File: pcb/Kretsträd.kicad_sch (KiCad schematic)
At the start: 56 parts, among them J1 Conn_01x02_Female, J2 Conn_01x02_Female, SW1 SW_PUSH, SW10 SW_PUSH, SW11 SW_PUSH, SW12 SW_PUSH, SW13 SW_PUSH, SW14 SW_PUSH, SW15 SW_PUSH, SW16 SW_PUSH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

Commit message: Traces completely re-routed.
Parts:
- removed Bat+_1, BatGND_1: MountingHole_Pad, kbd:1pin_conn, symbol Mechanical:MountingHole_Pad
- added J3: Conn_01x02_Female, Connector_Molex:Molex_PicoBlade_53047-0210_1x02_P1.25mm_Vertical, symbol Connector:Conn_01x02_Female
- added TH5: HOLE, MountingHole:MountingHole_3.2mm_M3, symbol SofleKeyboard-rescue:HOLE-Lily58-cache-Lily58_Pro-rescue
- D1, D10, D11, D12, D13, D14, D15, D16, D17, D2, D3, D4, D5, D6, D7, D8, D9: footprint jw_custom:Diode_SOD123_through_hole -> jw_custom_footprint:D_SOD123_THT
- J1: renamed from J2; footprint jw_custom_footprint:MOLEX_1x02_1.25mm_51146 -> Connector_Molex:Molex_Panelmate_53780-0270_1x02-1MP_P1.25mm_Horizontal
- J2: renamed from J1; footprint jw_custom_footprint:MOLEX_1x02_1.25mm_51146 -> Connector_Molex:Molex_Panelmate_53780-0270_1x02-1MP_P1.25mm_Horizontal
- JP2, JP3: value Hole_2 -> Hole_1
- JP4, JP5: value Hole_1 -> Hole_2
- SW_POWER_1, SW_POWER_2: footprint jw_custom_footprint:SPDT_C128955 -> Button_Switch_SMD:SW_SPDT_PCM12
- renumbered Hole_2 to Hole_1, Hole_1 to Hole_2
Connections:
- net Hole_1: now reaches Hole_1.1, JP2.1, JP3.1
- net Hole_1: now also J3.1 (Pin_1)
- net Hole_2: now reaches Hole_2.1, JP4.1, JP5.1
- net Hole_2: now also J3.2 (Pin_2)
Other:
- moved on the sheet: Hole_1, Hole_2, J2

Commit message: Tones of changes.
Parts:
- added JP1: to_RAW, Jumper:SolderJumper-2_P1.3mm_Open_RoundedPad1.0x1.5mm, symbol Device:Jumper_NO_Small
- D1, D10, D11, D12, D13, D14, D15, D16, D17, D2, D3, D4, D5, D6, D7, D8, D9: footprint jw_custom_footprint:D_SOD123_THT -> jw_custom_footprint:Diode_SOD123_THT_2
- JP2: renamed from JP1; footprint Jumper:SolderJumper-2_P1.3mm_Open_TrianglePad1.0x1.5mm -> Jumper:SolderJumper-2_P1.3mm_Open_RoundedPad1.0x1.5mm
- JP3: renamed from JP5; value Hole_2 -> Hole_1; footprint Jumper:SolderJumper-2_P1.3mm_Open_TrianglePad1.0x1.5mm -> Jumper:SolderJumper-2_P1.3mm_Open_RoundedPad1.0x1.5mm
- JP4: renamed from JP2; footprint Jumper:SolderJumper-2_P1.3mm_Open_TrianglePad1.0x1.5mm -> Jumper:SolderJumper-2_P1.3mm_Open_RoundedPad1.0x1.5mm
- JP5: renamed from JP4; footprint Jumper:SolderJumper-2_P1.3mm_Open_TrianglePad1.0x1.5mm -> Jumper:SolderJumper-2_P1.3mm_Open_RoundedPad1.0x1.5mm
- JP6: renamed from JP3; value Hole_1 -> Hole_2; footprint Jumper:SolderJumper-2_P1.3mm_Open_TrianglePad1.0x1.5mm -> Jumper:SolderJumper-2_P1.3mm_Open_RoundedPad1.0x1.5mm
- renumbered SW_POWER_1 to PWR_SW_1, SW_POWER_2 to PWR_SW_2
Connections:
- net Hole_1: now also JP3.1; no longer JP6.1
- net Hole_2: now also JP6.1; no longer JP3.1
- net RAW: now also JP1.2
- net at JP2.1, JP4.2, JP5.2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: now also JP1.1
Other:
- moved on the sheet: BT1, BT2, Hole_1, Hole_2, J1, J2, J3, JP2, JP3, JP4, JP5, JP6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

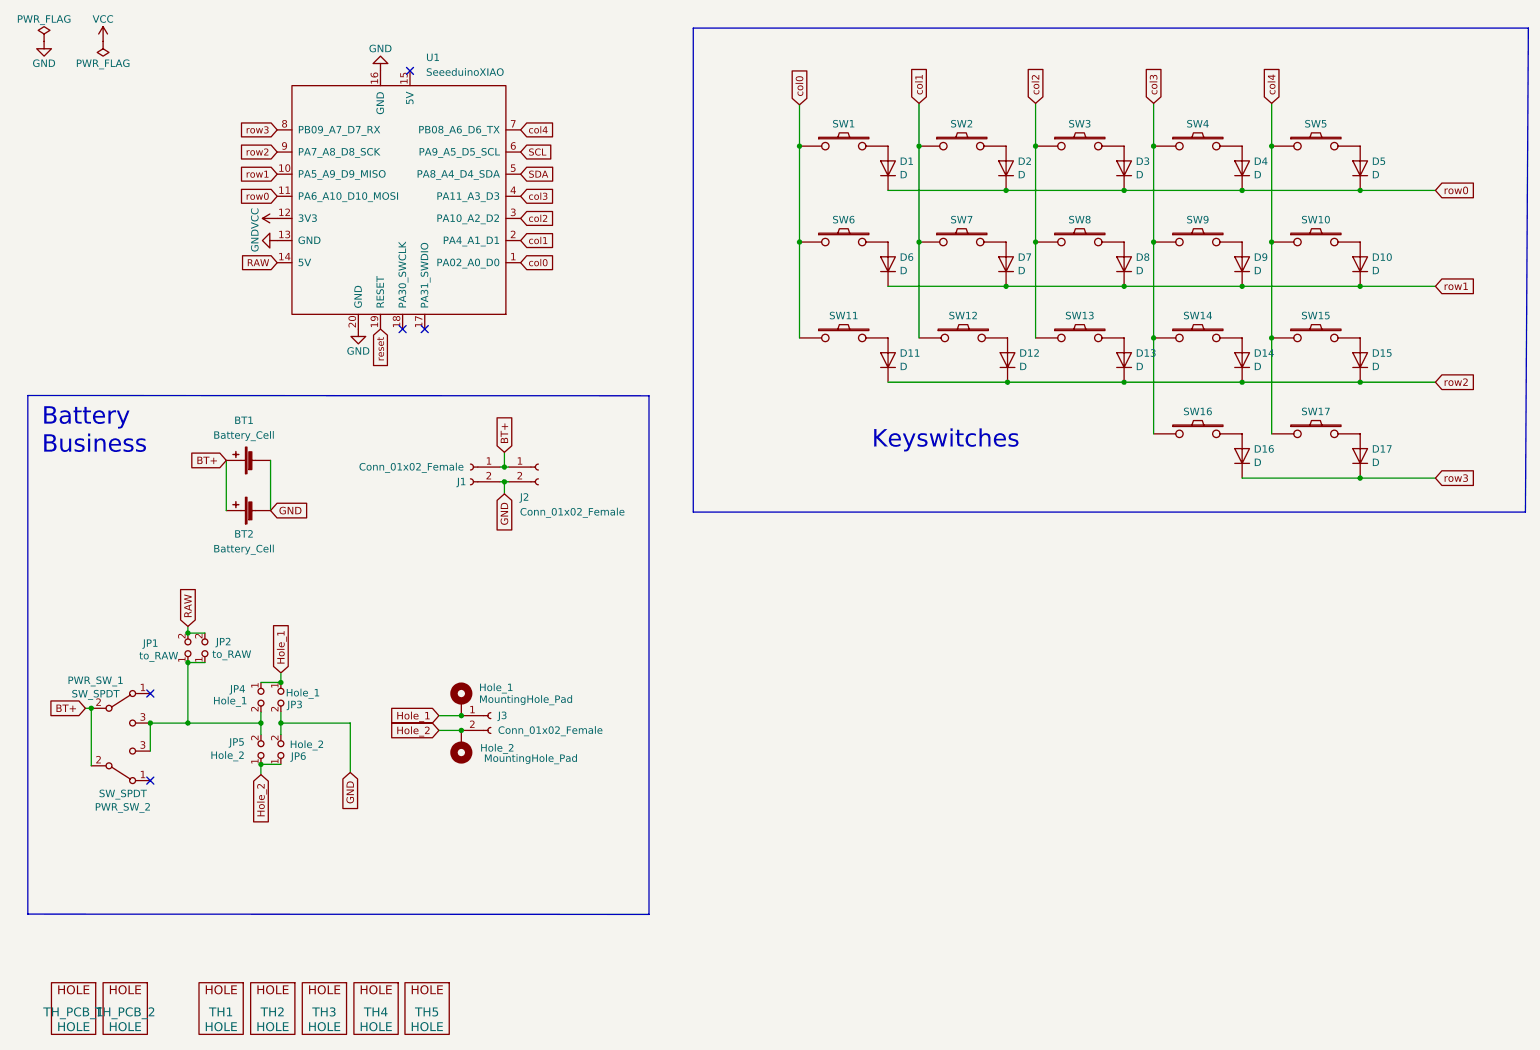
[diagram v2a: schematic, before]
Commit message: 1. Corrected all vias' size. 2. Minor change to circuit tree logo and text. 3. Other changes for aesthetics reasons.
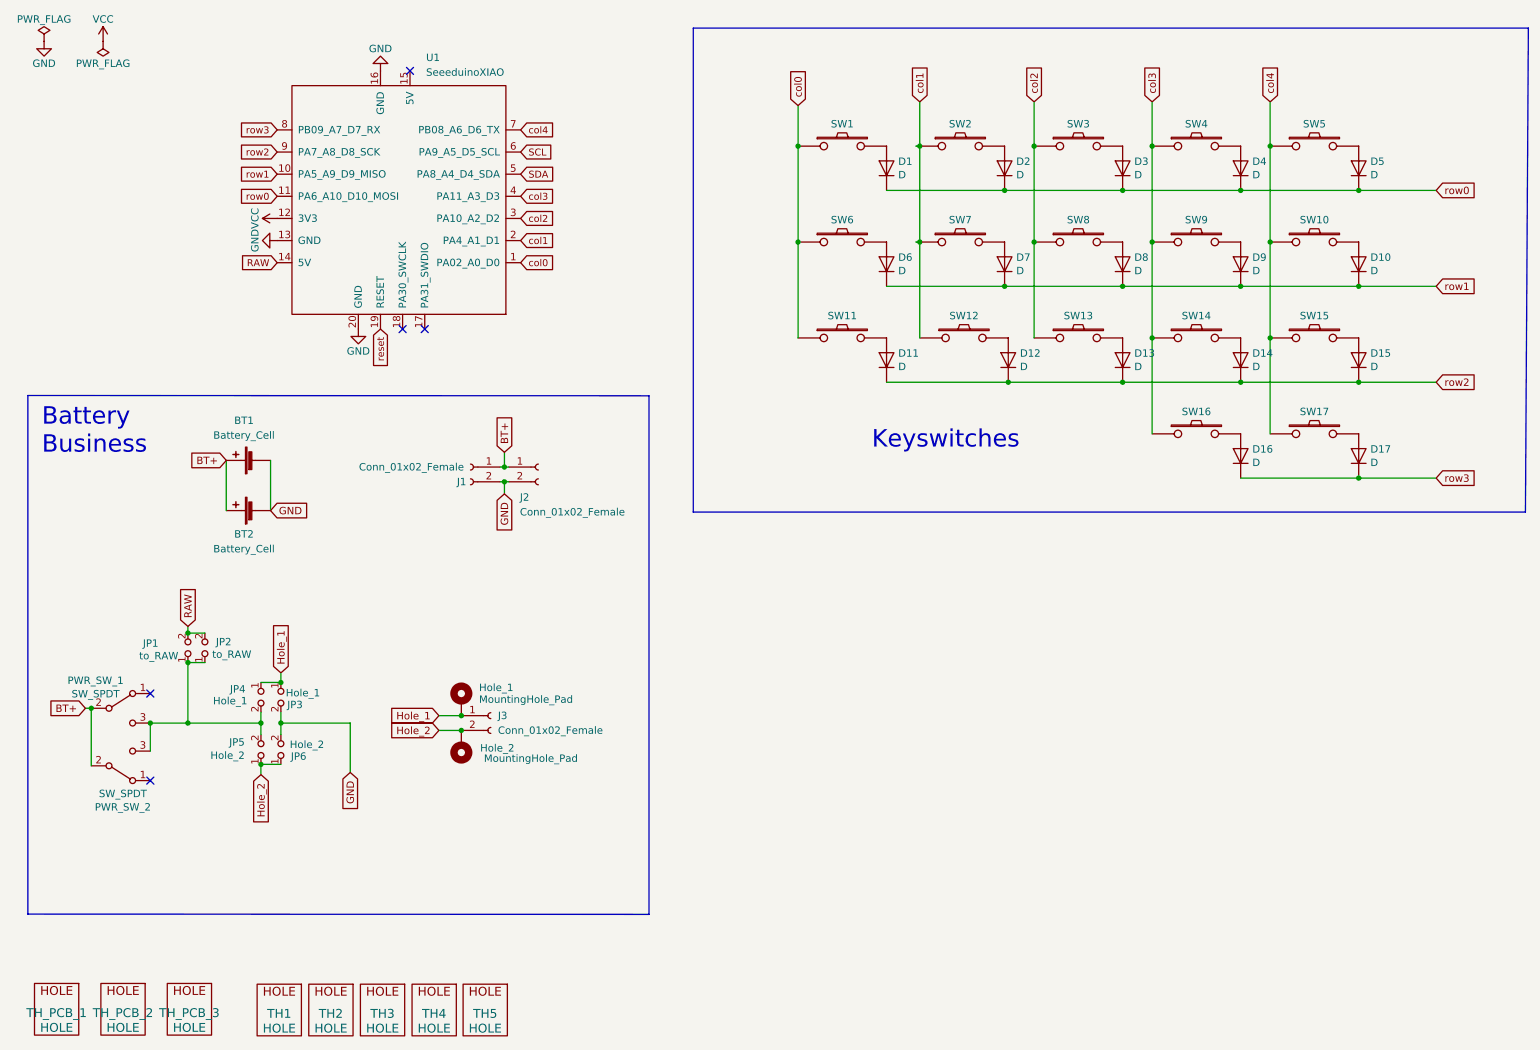
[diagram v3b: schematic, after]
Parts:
- added TH_PCB_3: HOLE, MountingHole:MountingHole_2.2mm_M2_Pad, symbol SofleKeyboard-rescue:HOLE-Lily58-cache-Lily58_Pro-rescue
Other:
- moved on the sheet: TH1, TH2, TH3, TH4, TH5, TH_PCB_1

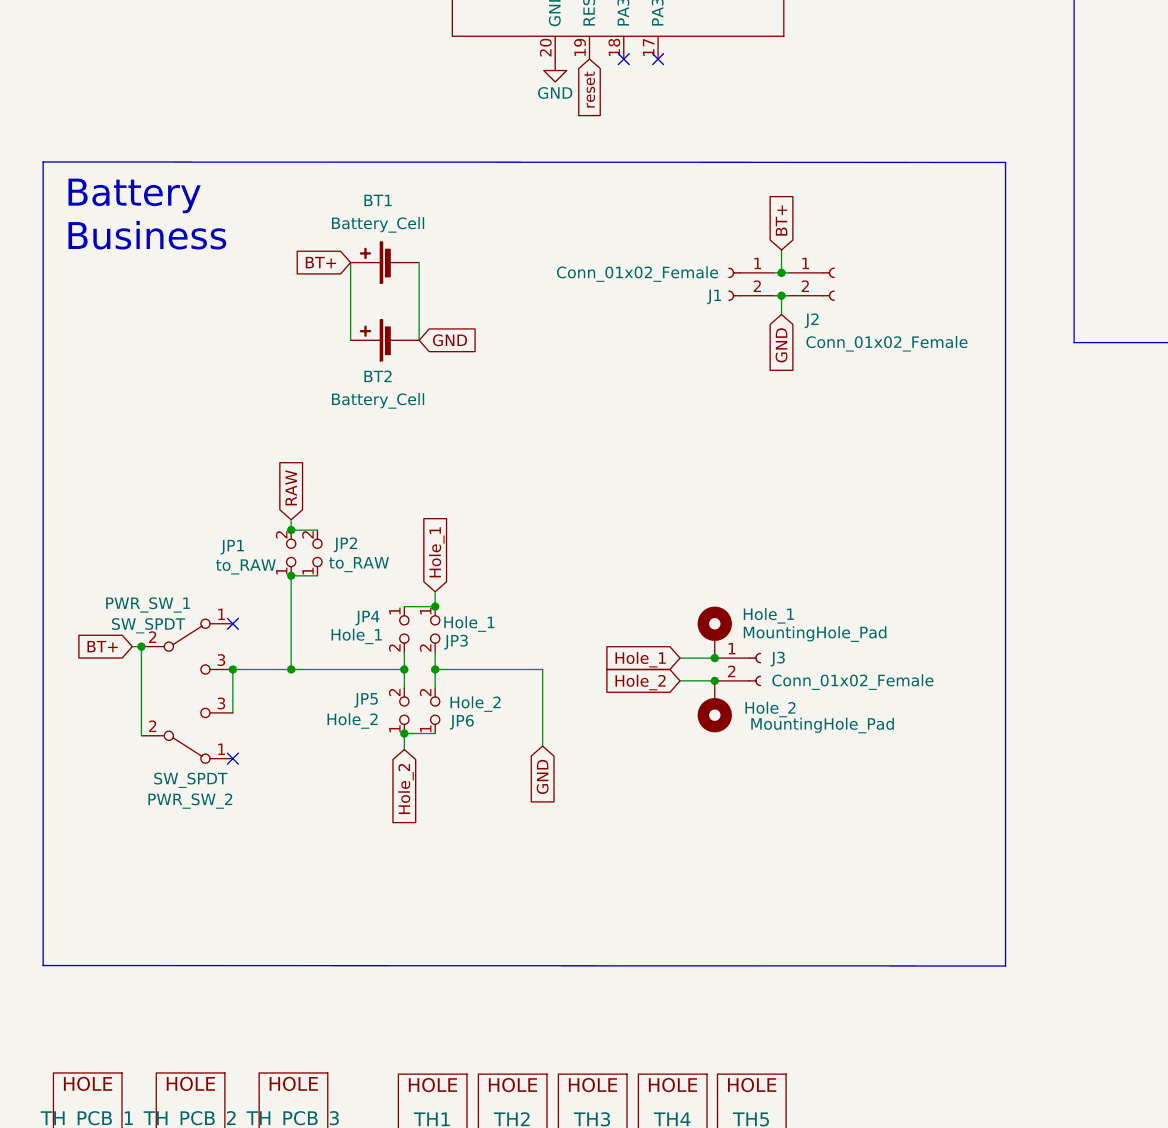
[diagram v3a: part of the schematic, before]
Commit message: 1. Modified LIR2032 battery holder footprint. 2. Changed Molex 1.25 battery female connector location. 3. Minor changes.
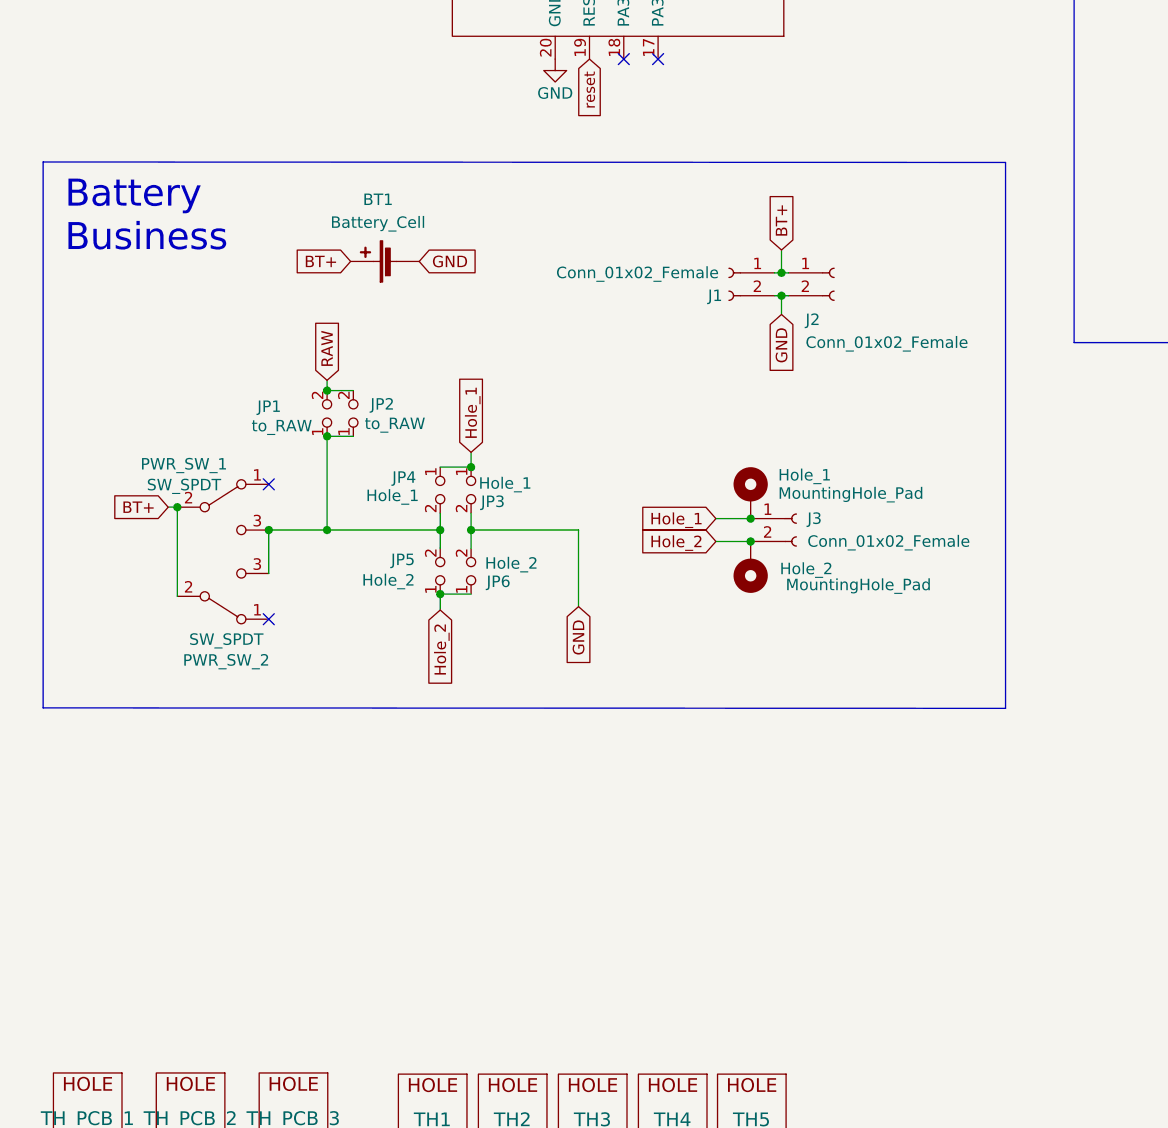
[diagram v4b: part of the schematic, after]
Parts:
- removed BT2: Battery_Cell, jw_custom_footprint:BatteryHolder_Keystone_3034_1x20mm_mod, symbol Device:Battery_Cell
- BT1: footprint jw_custom_footprint:BatteryHolder_Keystone_3034_1x20mm_mod -> jw_custom_footprint:BatteryHolder_Keystone_3034_1x20mm_mod_dual_side
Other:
- moved on the sheet: Hole_1, Hole_2, J3, JP1, JP2, JP3, JP4, JP5, JP6, PWR_SW_1, PWR_SW_2

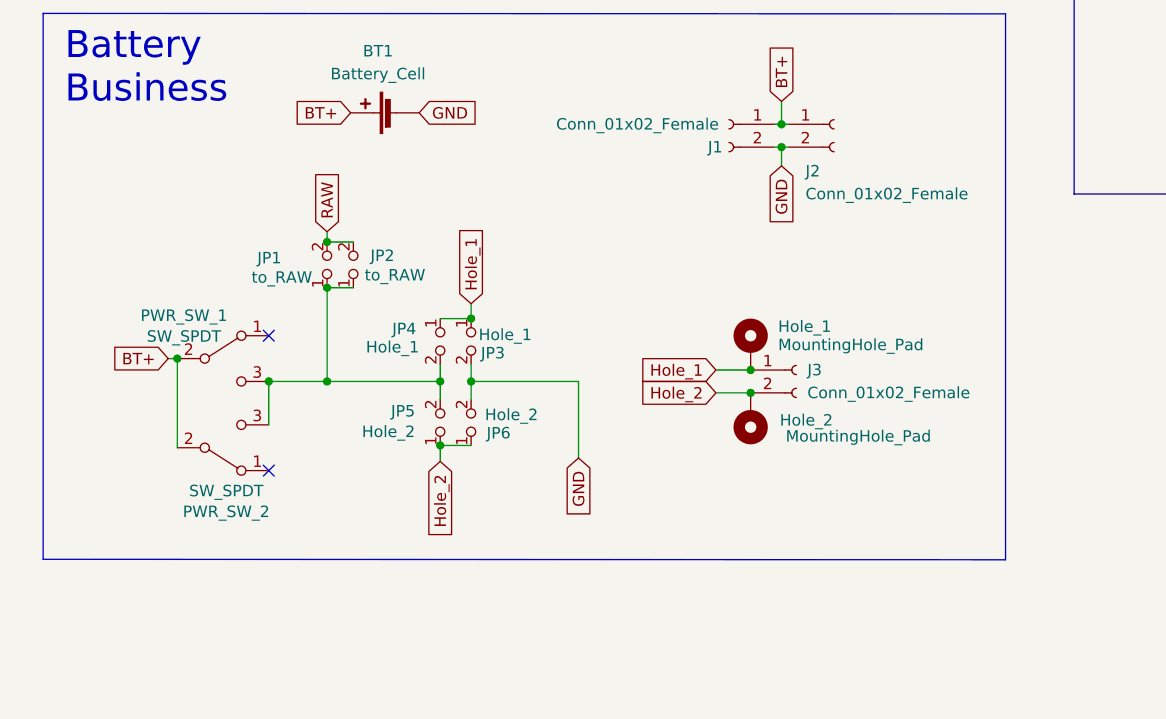
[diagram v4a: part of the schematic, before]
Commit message: 1. Updated switch footprint to increase solder pad size. 2. Squeezed MCU LIR2032 battery holder power switch section. 3. Re-routed a lot. 4. Reduced curvature on edge under thumb keys. 5. Removed power and ground pins selector jumper pads beneath MCU. 6. Other changes.
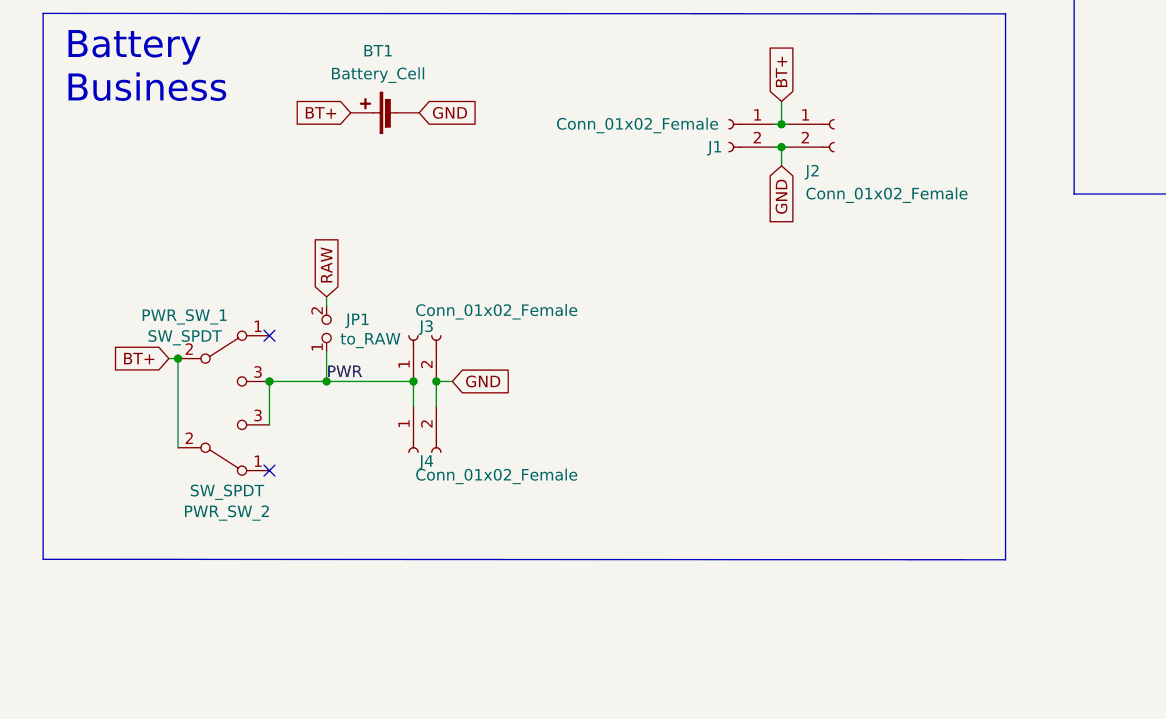
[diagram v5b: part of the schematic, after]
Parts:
- removed Hole_1, Hole_2: MountingHole_Pad, kbd:1pin_conn, symbol Mechanical:MountingHole_Pad
- removed JP2: to_RAW, Jumper:SolderJumper-2_P1.3mm_Open_RoundedPad1.0x1.5mm, symbol Device:Jumper_NO_Small
- removed JP3, JP4: Hole_1, Jumper:SolderJumper-2_P1.3mm_Open_RoundedPad1.0x1.5mm, symbol Device:Jumper_NO_Small
- removed JP5, JP6: Hole_2, Jumper:SolderJumper-2_P1.3mm_Open_RoundedPad1.0x1.5mm, symbol Device:Jumper_NO_Small
- added J4: Conn_01x02_Female, Connector_PinSocket_2.54mm:PinSocket_1x02_P2.54mm_Vertical, symbol Connector:Conn_01x02_Female
- JP1: footprint Jumper:SolderJumper-2_P1.3mm_Open_RoundedPad1.0x1.5mm -> jw_custom_footprint:SolderJumper-2_P1.3mm_Open_RoundedPad1.0x1.5mm_dual_side
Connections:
- net Hole_1 is gone; now on net PWR: J3.1 (Pin_1)
- net Hole_2 is gone; now on net GND: J3.2 (Pin_2)
- net GND: now also J4.2 (Pin_2)
- net PWR: now reaches JP1.1, PWR_SW_1.3 (C), PWR_SW_2.3 (C)
- net PWR: now also J4.1 (Pin_1)
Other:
- moved on the sheet: J3, JP1
